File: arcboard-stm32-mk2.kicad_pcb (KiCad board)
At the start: 2 copper layers, 60 x 60 mm, 90 parts, among them J1 Conn_01x04_Socket, J17 Conn_01x04_Socket, J2 Conn_01x04_Socket, J3 Conn_01x04_Socket, J4 Conn_01x02_Socket, J5 Conn_01x02_Socket, J6 Conn_01x02_Socket, J7 Conn_01x02_Socket, J8 Conn_01x02_Socket, U1 XC6210B332MR-G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

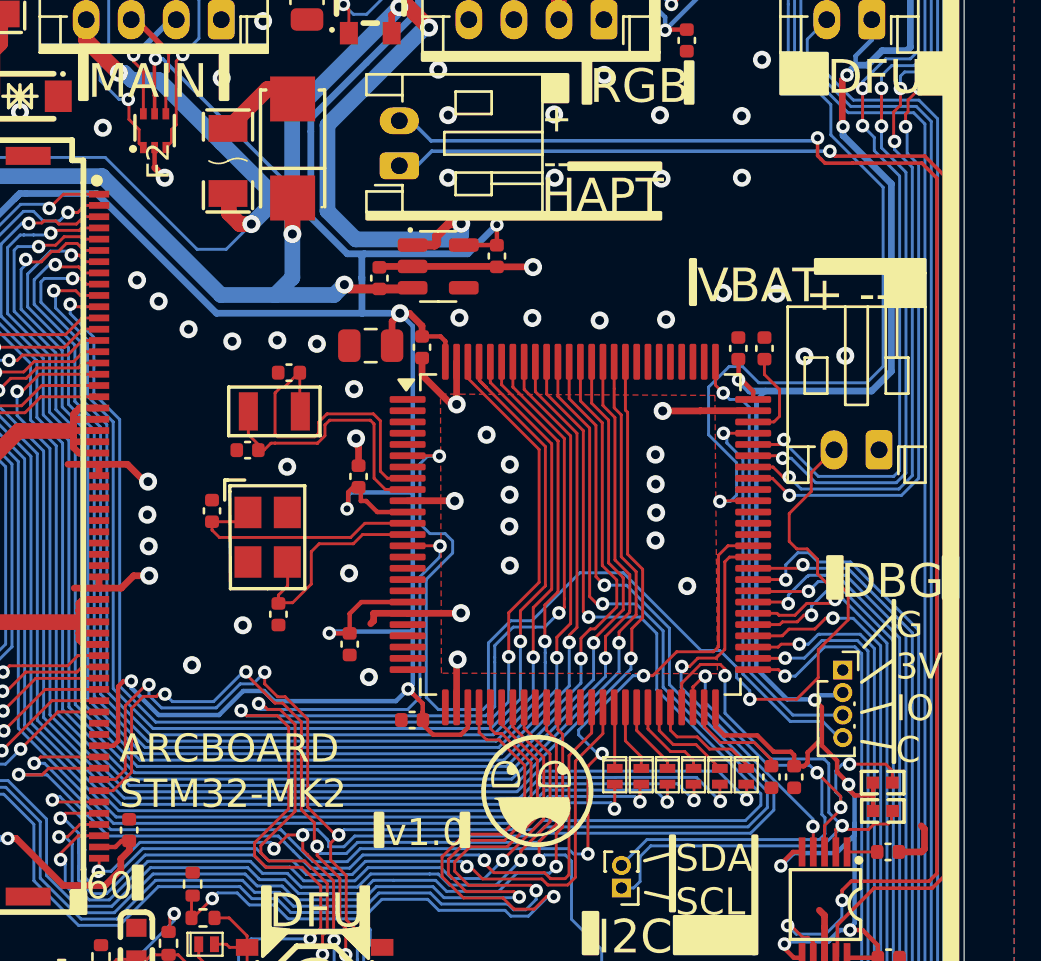
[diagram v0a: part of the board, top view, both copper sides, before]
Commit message: fixing i2c resistors, prepping for 10pin
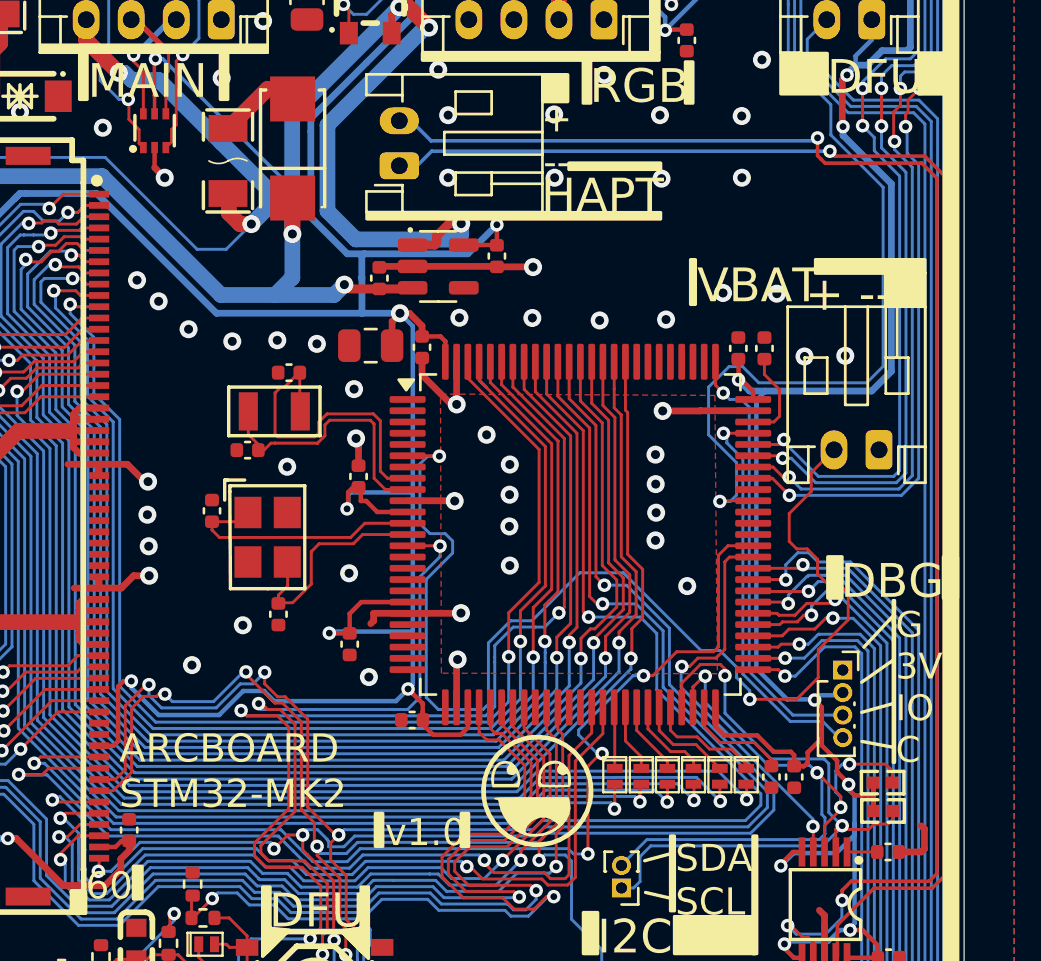
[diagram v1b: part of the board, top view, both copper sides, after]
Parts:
- removed R13: 0402WGF2201TCE, kicad-libraries:R0402
- added R7: 0402WGF4701TCE, kicad-libraries:R0402, F.Cu at (126.4, 112.7)
- R4: value 0402WGF2201TCE -> 0402WGF4701TCE

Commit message: bunch o updates
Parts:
- removed J8: Conn_01x02_Socket, Connector_JST:JST_PH_S2B-PH-K_1x02_P2.00mm_Horizontal
- added J9: Conn_01x10_Socket, Connector_JST:JST_PH_S10B-PH-K_1x10_P2.00mm_Horizontal, F.Cu at (125.7, 77.5)
- added R8: 0402WGF4701TCE, kicad-libraries:R0402, F.Cu at (118.3, 85.7)
- J3: value Conn_01x04_Socket -> Conn_01x01; footprint Connector_JST:JST_PH_S4B-PH-K_1x04_P2.00mm_Horizontal -> TestPoint:TestPoint_Pad_1.5x1.5mm
- J5, J7: value Conn_01x02_Socket -> Conn_01x01; footprint Connector_JST:JST_PH_S2B-PH-K_1x02_P2.00mm_Horizontal -> TestPoint:TestPoint_Pad_1.5x1.5mm
- moved J3 25.1 mm to (124.5, 100.2), turned to 0 degrees
- moved J7 22.6 mm to (124.5, 95.2), turned to 0 degrees
- moved J5 20.3 mm to (124.5, 97.8), turned to 0 degrees
- moved C18 13.2 mm to (116.0, 86.2), turned to -90 degrees
- moved LED-LVL1 12.2 mm to (114.3, 85.2)
- moved C19 9.28 mm to (112.5, 86.2)
- moved C8 2.27 mm to (121.7, 109.0), turned to -90 degrees
- moved C23 0.64 mm to (100.8, 73.6)
- moved C7 0.55 mm to (120.5, 92.1)
- moved C21 0.47 mm to (121.6, 92.1)
- moved C20 0.45 mm to (100.8, 77.0)
- moved C1 0.37 mm to (103.6, 72.9), turned to -90 degrees
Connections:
- C1 pad 1: RGB_5V -> GND
- C1 pad 2: GND -> RGB_5V
- D11 pad 2: Net-(D11-A) -> DFU
- J3 pad 1: GND -> SPARE1
- J5 pad 1: +3V3 -> SPARE2
- J7 pad 1: HAPTIC_neg -> SPARE3
- R15 pad 1: Net-(D11-A) -> DFU
- U15 pad 4: Net-(D11-A) -> DFU
- U2 pad 63: unconnected-(U2-PC6-Pad63) -> LIMIT1
- U2 pad 64: unconnected-(U2-PC7-Pad64) -> SPARE1
- U2 pad 65: unconnected-(U2-PC8-Pad65) -> SPARE2
- U2 pad 67: unconnected-(U2-PA8-Pad67) -> SPARE3
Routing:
- net DFU: track 0.00 -> 99.3 mm, vias 0 -> 5
- net Net-(D11-A): track 95.0 -> 0.00 mm, vias 3 -> 0
- net LIMIT1: track 0.00 -> 43.6 mm, vias 0 -> 2
- net VBAT: track 52.4 -> 82.2 mm, vias 2 -> 1
- net RGB_5V: track 122.4 -> 143.1 mm, vias 5 -> 7
- net LED_EXT_DI: track 161.7 -> 146.2 mm
- net +5V: track 117.6 -> 102.5 mm, vias 11 -> 10
- net +3V3: track 385.8 -> 398.1 mm, vias 26 -> 27
- net SPARE3: track 0.00 -> 7.54 mm
- net GND: track 55.6 -> 61.6 mm, vias 67 -> 64
- net SPARE2: track 0.00 -> 5.16 mm
- net VBUS: track 130.1 -> 134.4 mm
- net SPARE1: track 0.00 -> 3.95 mm
- net LED_SIG_OUTPUT: track 39.2 -> 36.6 mm, vias 2 -> 4
- net SWCLK: track 19.6 -> 22.0 mm
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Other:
- board text added: "- STM32F407 - 16MB SPI Flash - Haptic DRV2605L - DAC Amp PAM8302A - 32MHz LSE for RTC - VBAT 1.6-3.3v"
- board text added: "5V DP DM GND"
- board text added: "GND TX RX VBUS"
- board text added: "HAP+ HAP- VBAT LIM GND 3V3 DFU LED 5V GND"
- board text added: "HARN"
- board text added: "SP1"
- board text added: "SP2"
- board text added: "SP3"
- board text added: "WIRING HARNESS MAIN USB SPLIT USB"
- board text removed: "+ --"
- board text removed: "- STM32F405 - 16MB SPI Flash - Haptic DRV2605L - DAC Amp PAM8302A - 32MHz LSE for RTC - VBAT 1.6-3.3v"
- board text removed: "BOOT/RESET 3V3 DFU"
- board text removed: "EXT RGB G 5V LED x"
- board text removed: "HAP+ HAP-"
- board text removed: "HAPT"
- board text removed: "MAIN USB G DM DP 5V"
- board text removed: "RGB"
- board text removed: "SPLIT USB G TX RX VBUS"
- board text removed: "Using JST-PH connectors"
- board text removed: "VBAT"
